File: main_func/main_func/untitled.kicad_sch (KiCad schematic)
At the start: 0 parts

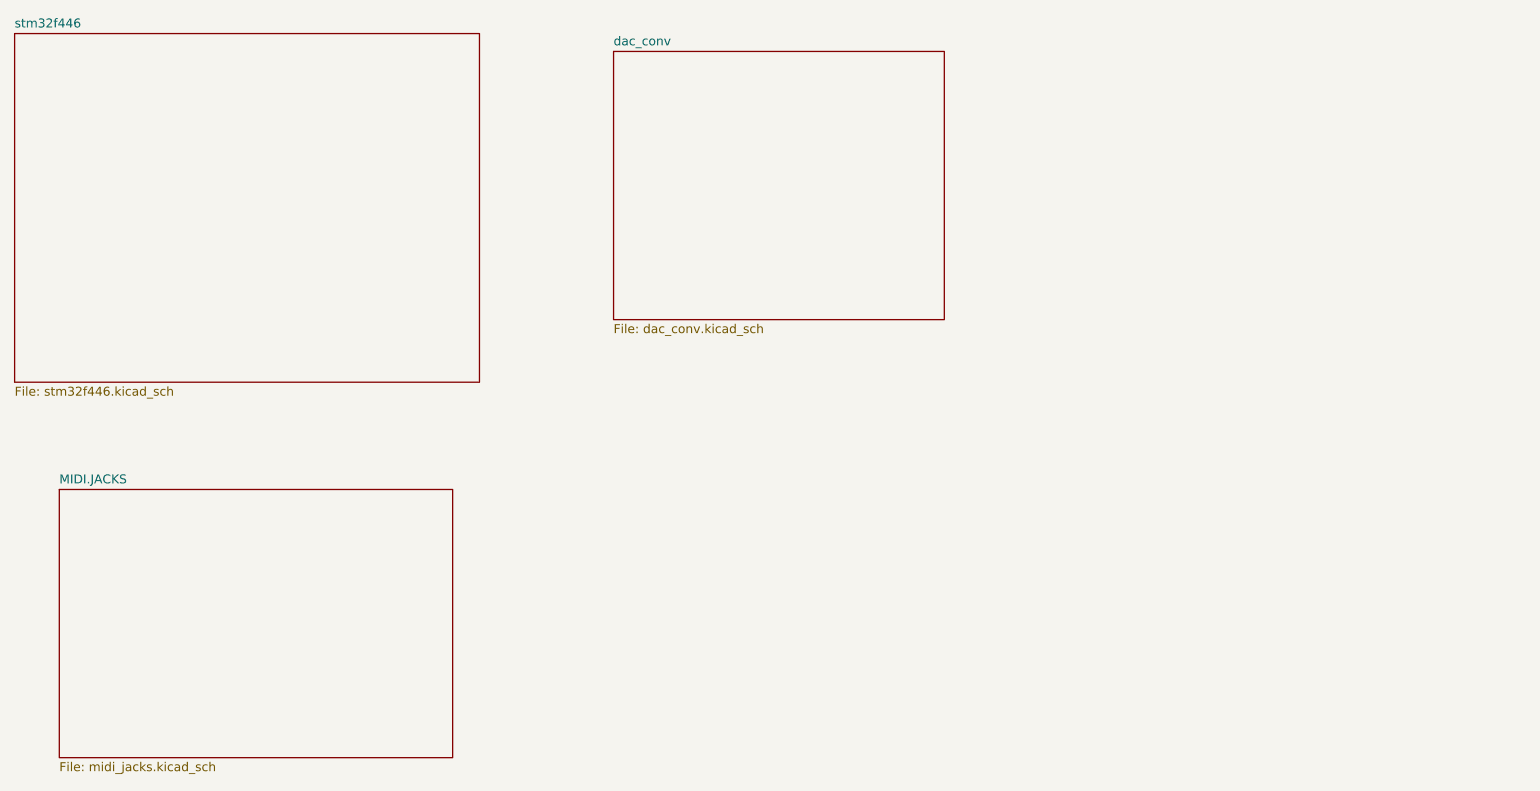
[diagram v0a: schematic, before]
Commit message: main func schematics fixed
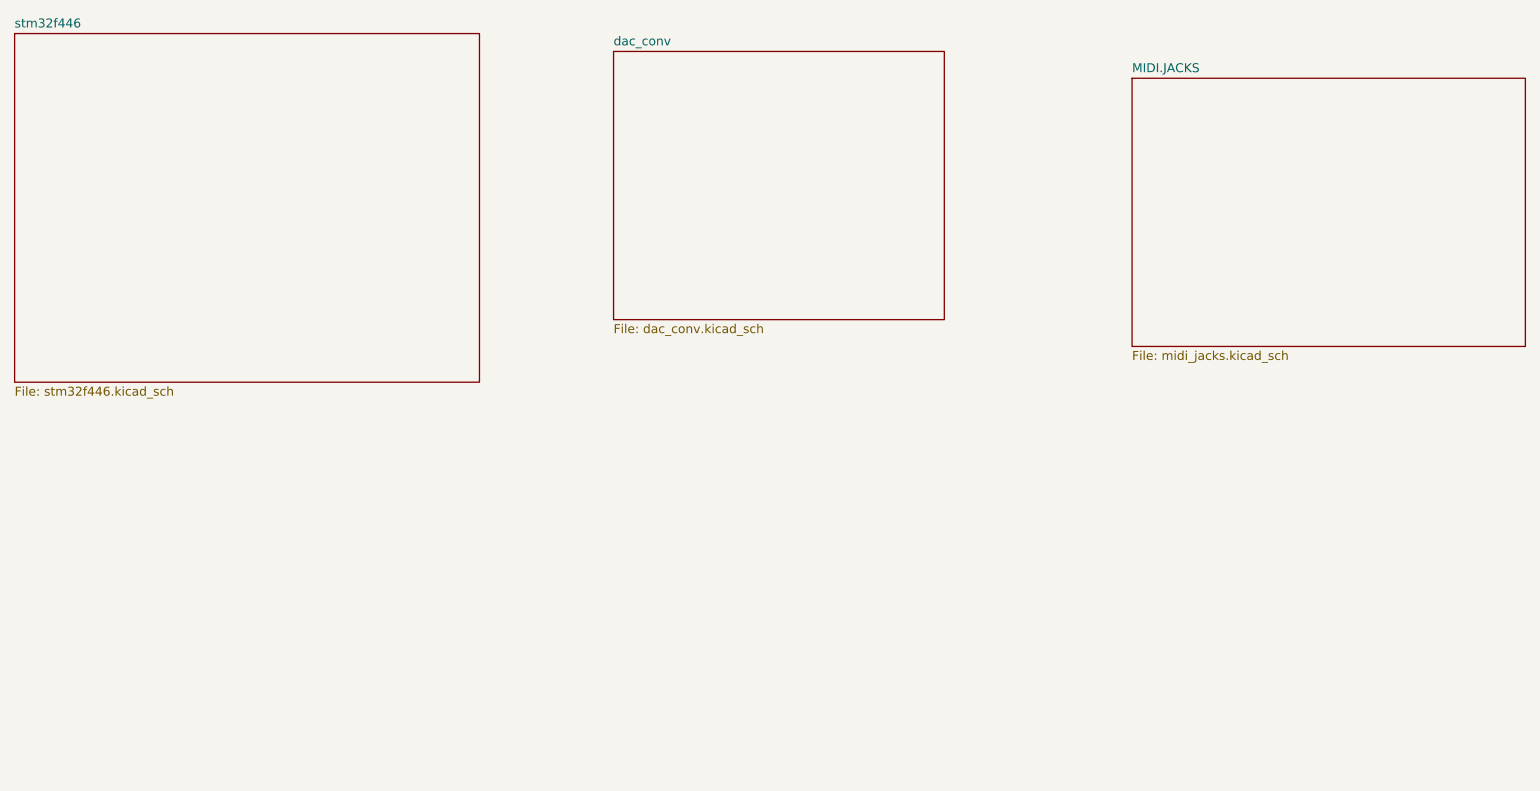
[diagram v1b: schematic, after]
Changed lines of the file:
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@@
     )
   )
-  (sheet (at 46.99 93.98) (size 55.88 38.1) (fields_autoplaced)
+  (sheet (at 199.39 35.56) (size 55.88 38.1) (fields_autoplaced)
     (stroke (width 0.1524) (type solid) (color 0 0 0 0))
     (fill (color 0 0 0 0.0000))
-    (property "Sheet name" "MIDI.JACKS" (id 0) (at 46.99 93.2684 0)
+    (property "Sheet name" "MIDI.JACKS" (id 0) (at 199.39 34.8484 0)
       (effects (font (size 1.27 1.27)) (justify left bottom))
     )
-    (property "Sheet file" "midi_jacks.kicad_sch" (id 1) (at 46.99 132.6646 0)
+    (property "Sheet file" "midi_jacks.kicad_sch" (id 1) (at 199.39 74.2446 0)
       (effects (font (size 1.27 1.27)) (justify left top))
     )
